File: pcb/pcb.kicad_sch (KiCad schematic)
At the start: 35 parts, among them J1 DIN-5_180degree, J5 Barrel_Jack, J6 Barrel_Jack, U1 MCP3008, U2 MCP3008

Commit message: completed circuit design
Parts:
- removed J5, J6, To_Main_Out: Barrel_Jack, symbol Connector:Barrel_Jack
- added C1, C2: C, symbol Device:C
- added J2: Conn_02x06_Odd_Even, Connector_PinHeader_2.54mm:PinHeader_2x06_P2.54mm_Horizontal, symbol Connector_Generic:Conn_02x06_Odd_Even
- added J3: Conn_02x02_Odd_Even, Connector_PinHeader_2.54mm:PinHeader_2x02_P2.54mm_Horizontal, symbol Connector_Generic:Conn_02x02_Odd_Even
- added R1: 220, symbol Device:R
- added R2: 270, symbol Device:R
- added U4: H11L1M, digikey-footprints:DIP-6_W7.62mm, symbol dk_Optoisolators-Logic-Output:H11L1M
- Bit_Crush_In1: renamed from Bit_Crush_In; symbol Connector:Barrel_Jack -> Connector_Audio:AudioJack2
- Bit_Crush_Out1: renamed from Bit_Crush_Out; symbol Connector:Barrel_Jack -> Connector_Audio:AudioJack2
- Delay_In1: renamed from Delay_In; symbol Connector:Barrel_Jack -> Connector_Audio:AudioJack2
- Delay_Out1: renamed from Delay_Out; symbol Connector:Barrel_Jack -> Connector_Audio:AudioJack2
- Distortion_In1: renamed from Distortion_In; symbol Connector:Barrel_Jack -> Connector_Audio:AudioJack2
- Distortion_Out1: renamed from Distortion_Out; symbol Connector:Barrel_Jack -> Connector_Audio:AudioJack2
- Filter_In1: renamed from Filter_In; symbol Connector:Barrel_Jack -> Connector_Audio:AudioJack2
- Filter_Out1: renamed from Filter_Out; symbol Connector:Barrel_Jack -> Connector_Audio:AudioJack2
- From_Sample1: renamed from From_Sample; symbol Connector:Barrel_Jack -> Connector_Audio:AudioJack2
- Reverb_In1: renamed from Reverb_In; symbol Connector:Barrel_Jack -> Connector_Audio:AudioJack2
- Reverb_Out1: renamed from Reverb_Out; symbol Connector:Barrel_Jack -> Connector_Audio:AudioJack2
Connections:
- net +3.3V: now also C1.1, C2.1, J2.1 (Pin_1), J2.2 (Pin_2), R2.1, U4.6 (VCC)
- net GND: now also C1.2, C2.2, J2.3 (Pin_3), J2.4 (Pin_4), U4.5 (GND)
- net at J1.4: now also R1.1
- net at J1.5: now also D3.2 (A), U4.2
- net at D3.1 (K): now also R1.2, U4.1
- net at U2.10 (~{CS}/SHDN): now also J2.6 (Pin_6)
- net at U1.11 (Din), U2.11 (Din): now also J3.4 (Pin_4)
- net at U1.12 (Dout), U2.12 (Dout): now also J3.3 (Pin_3)
- net at U1.13 (CLK), U2.13 (CLK): now also J3.1 (Pin_1)
- net at U1.10 (~{CS}/SHDN): now also J2.5 (Pin_5)
- new net: D2.1 (K), Reverb_In1.S, Reverb_In1.T
- new net: D6.1 (K), Distortion_In1.S, Distortion_In1.T
- new net: D6.2 (A), Distortion_Out1.S, Distortion_Out1.T, J2.10 (Pin_10)
- new net: J3.2 (Pin_2), R2.2, U4.4 (VO)
- new net: D5.1 (K), Filter_In1.S, Filter_In1.T
- new net: D5.2 (A), Filter_Out1.S, Filter_Out1.T, J2.8 (Pin_8)
- new net: D1.1 (K), Delay_In1.S, Delay_In1.T
- new net: D1.2 (A), Delay_Out1.S, Delay_Out1.T, J2.11 (Pin_11)
- new net: Bit_Crush_In1.S, Bit_Crush_In1.T, D4.1 (K)
- new net: Bit_Crush_Out1.S, Bit_Crush_Out1.T, D4.2 (A), J2.7 (Pin_7)
- new net: From_Sample1.S, From_Sample1.T, J2.12 (Pin_12)
- new net: D2.2 (A), J2.9 (Pin_9), Reverb_Out1.S, Reverb_Out1.T
- no-connect marks 6 -> 7
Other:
- moved on the sheet: D1, D2, J1

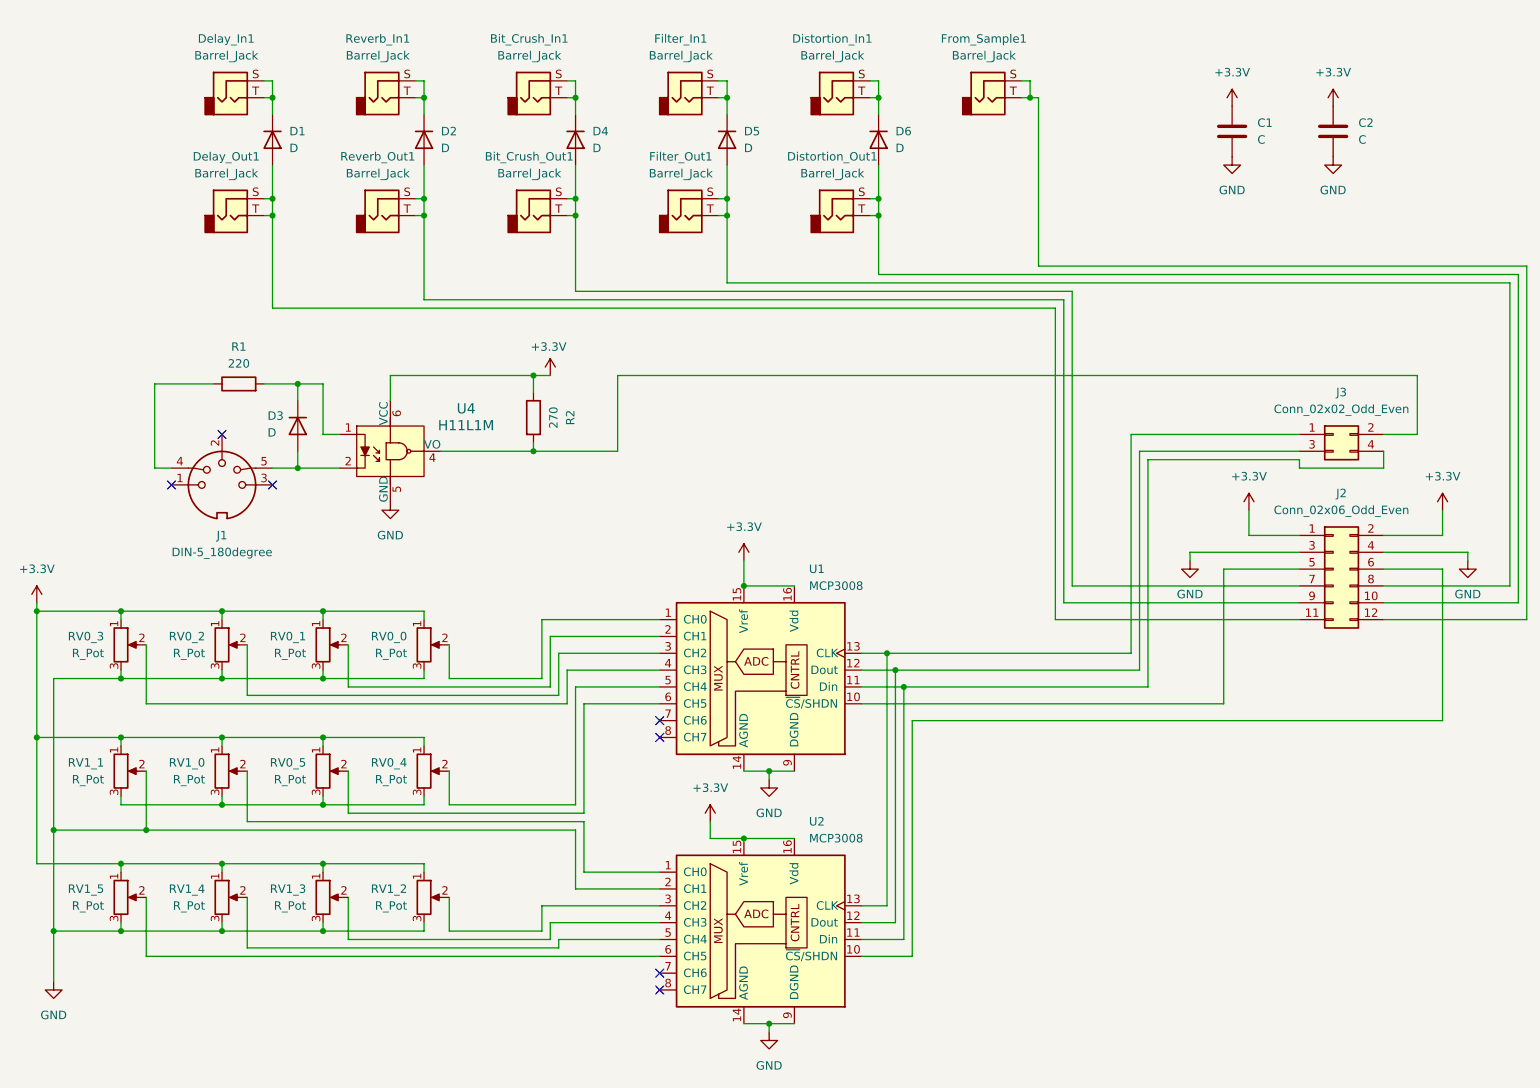
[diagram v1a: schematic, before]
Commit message: added footprints to pcb and updated gitignore to include kicad.gitignore
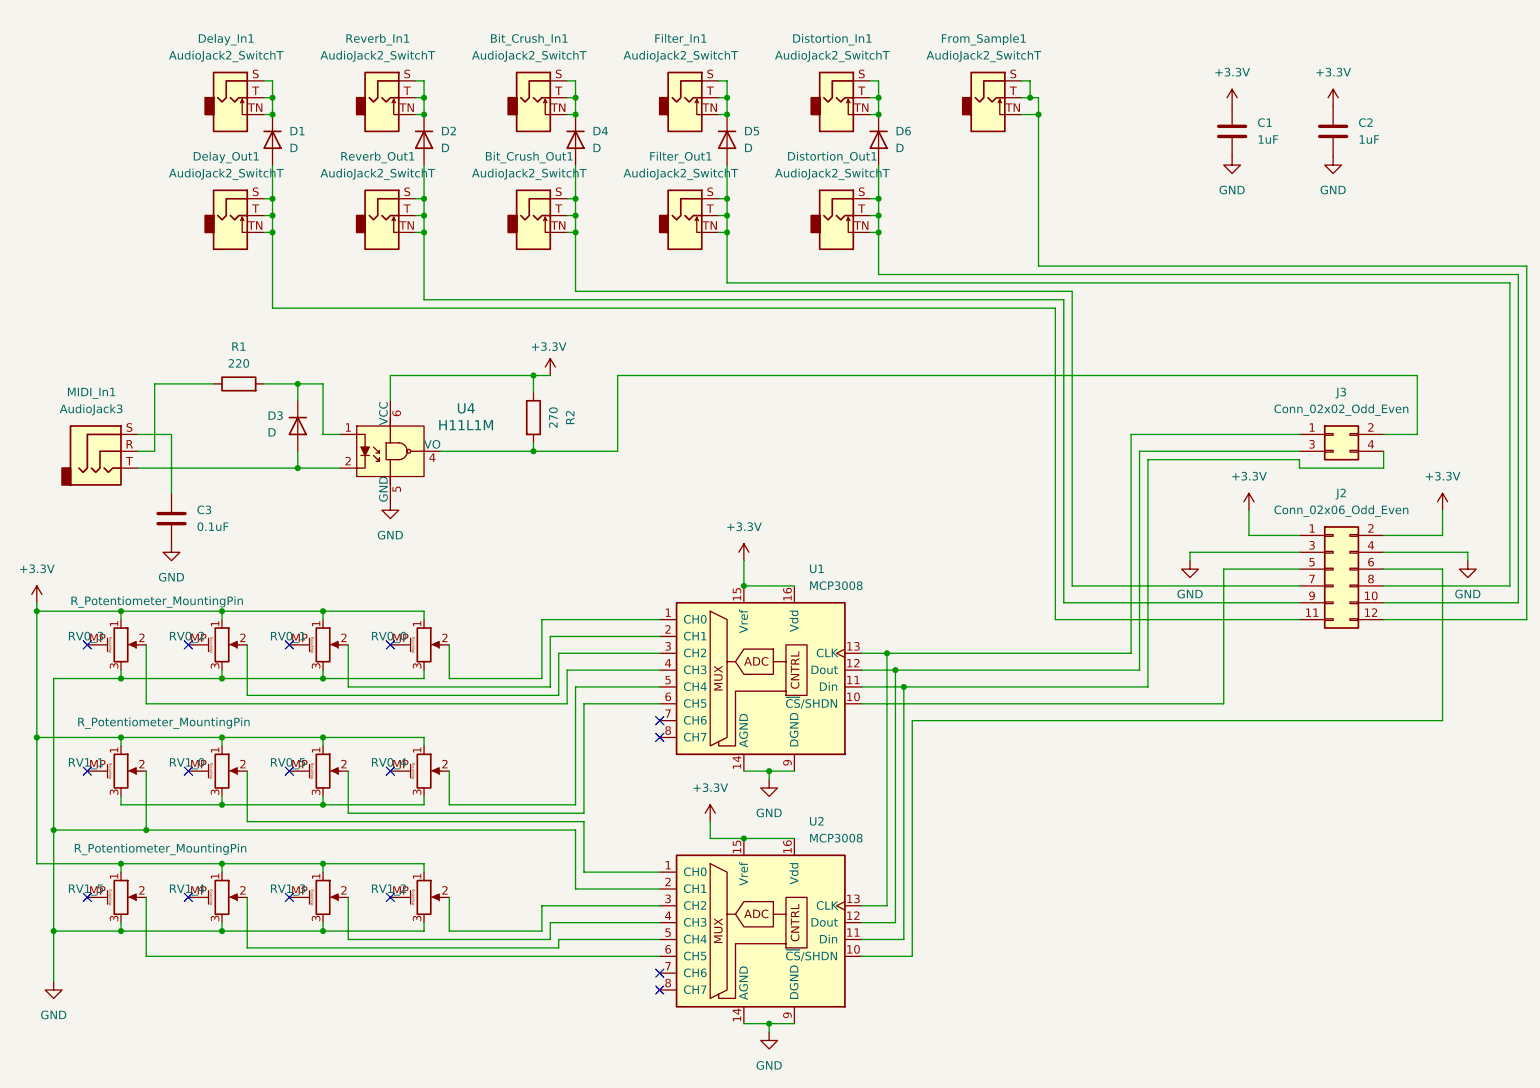
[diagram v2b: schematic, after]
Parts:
- removed J1: DIN-5_180degree, symbol Connector:DIN-5_180degree
- added C3: 0.1uF, digikey-footprints:0805, symbol Device:C
- added MIDI_In1: AudioJack3, My_Library:Jack_3.5mm_QingPu_WQP-PJ366ST_Vertical_CircularHoles, symbol Connector_Audio:AudioJack3
- Bit_Crush_In1, Bit_Crush_Out1, Delay_In1, Delay_Out1, Distortion_In1, Distortion_Out1, Filter_In1, Filter_Out1, From_Sample1, Reverb_In1, Reverb_Out1: value Barrel_Jack -> AudioJack2_SwitchT; footprint (none) -> Jack_3.5mm_QingPu_WQP-PJ398SM_Vertical_CircularHoles; symbol Connector_Audio:AudioJack2 -> Connector_Audio:AudioJack2_SwitchT
- C1, C2: value C -> 1uF; footprint (none) -> digikey-footprints:0805
- D1, D2, D3, D4, D5, D6, R1, R2: footprint (none) -> digikey-footprints:0805
- RV0_0, RV0_1, RV0_2, RV0_3, RV0_4, RV0_5, RV1_0, RV1_1, RV1_2, RV1_3, RV1_4, RV1_5: value R_Pot -> R_Potentiometer_MountingPin; footprint (none) -> My_Library:Potentiometer_Alpha_RD901F-40-00D_Single_Vertical_MP; symbol Device:R_Potentiometer -> Device:R_Potentiometer_MountingPin
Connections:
- net GND: now also C3.2
- net at D2.1 (K), Reverb_In1.S, Reverb_In1.T: now also Reverb_In1.TN
- net at R1.1: now also MIDI_In1.R
- net at D3.2 (A), U4.2: now also MIDI_In1.T
- net at D6.1 (K), Distortion_In1.S, Distortion_In1.T: now also Distortion_In1.TN
- net at D6.2 (A), Distortion_Out1.S, Distortion_Out1.T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: now also Distortion_Out1.TN
- net at D5.1 (K), Filter_In1.S, Filter_In1.T: now also Filter_In1.TN
- net at D5.2 (A), Filter_Out1.S, Filter_Out1.T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: now also Filter_Out1.TN
- net at D1.1 (K), Delay_In1.S, Delay_In1.T: now also Delay_In1.TN
- net at D1.2 (A), Delay_Out1.S, Delay_Out1.T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: now also Delay_Out1.TN
- net at Bit_Crush_In1.S, Bit_Crush_In1.T, D4.1 (K): now also Bit_Crush_In1.TN
- net at Bit_Crush_Out1.S, Bit_Crush_Out1.T, D4.2 (A)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: now also Bit_Crush_Out1.TN
- net at From_Sample1.S, From_Sample1.T, J2.12 (Pin_12): now also From_Sample1.TN
- net at D2.2 (A), J2.9 (Pin_9), Reverb_Out1.S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: now also Reverb_Out1.TN
- new net: C3.1, MIDI_In1.S
- no-connect marks 7 -> 16

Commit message: layed out pcb and adjusted design to meet Spartan 7 GPIO spec
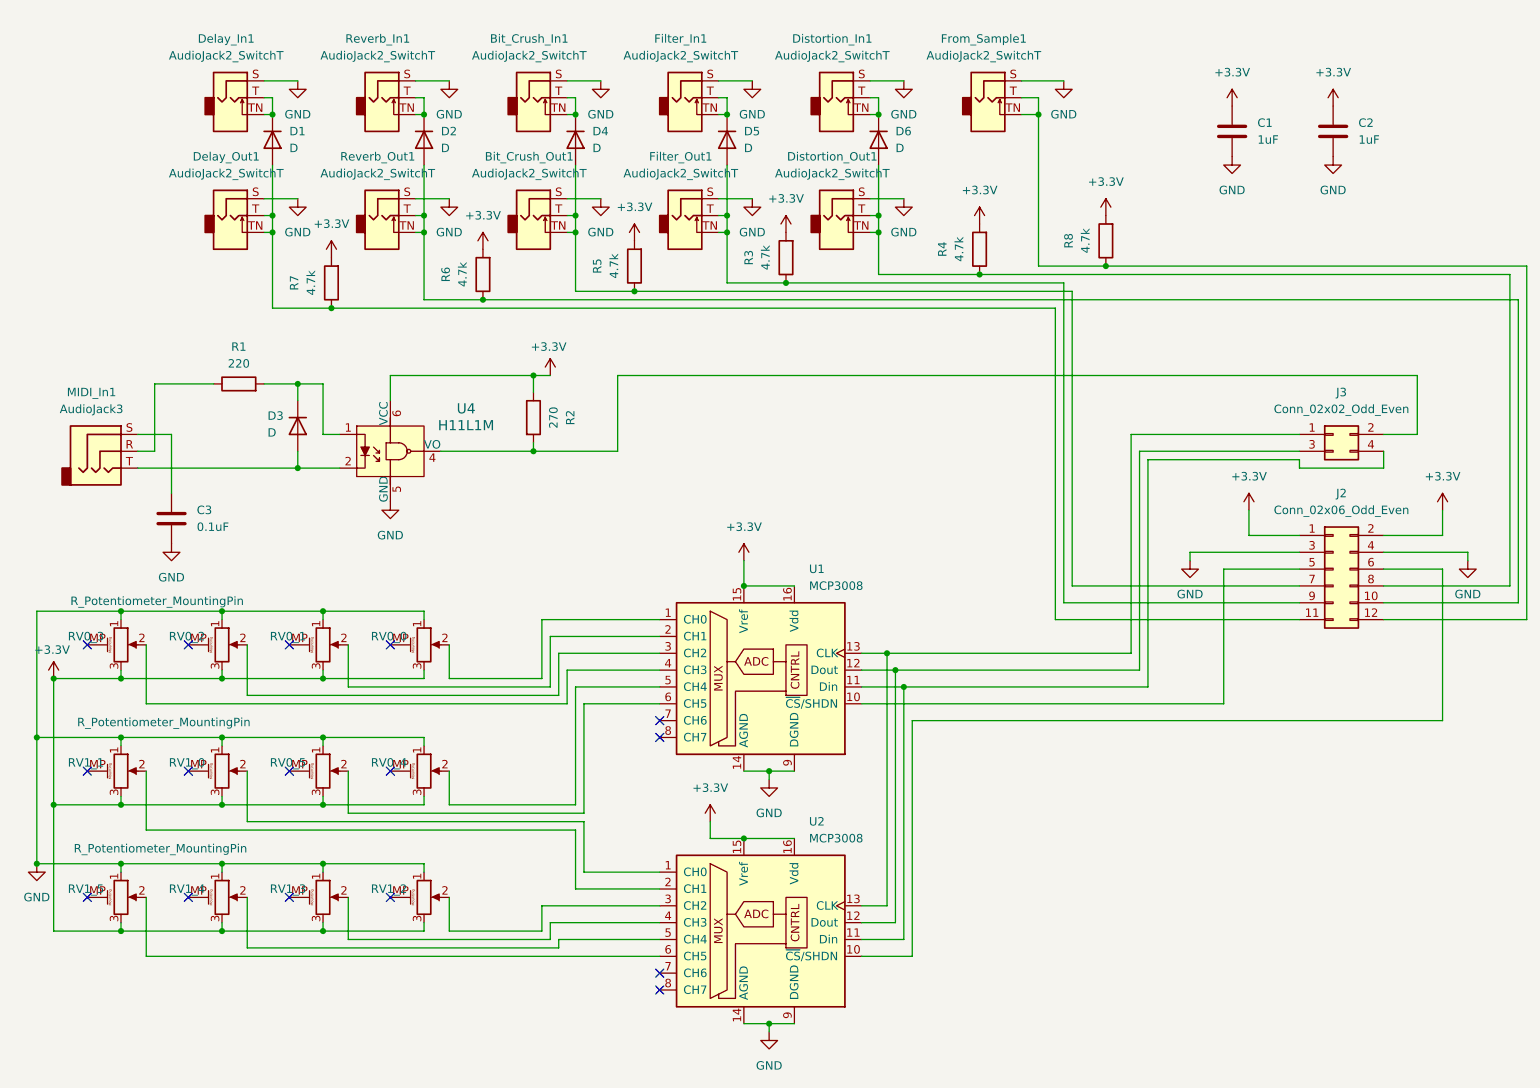
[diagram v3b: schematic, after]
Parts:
- added R3, R4, R5, R6, R7, R8: 4.7k, digikey-footprints:0805, symbol Device:R
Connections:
- net +3.3V: now also RV0_0.3, RV0_1.3, RV0_2.3, RV0_3.3, RV0_4.3, RV0_5.3, RV1_0.3, RV1_1.3, RV1_2.3, RV1_3.3, RV1_4.3, RV1_5.3, R3.2, R4.2, R5.2, R6.2, R7.2, R8.2; no longer RV0_0.1, RV0_1.1, RV0_2.1, RV0_3.1, RV0_4.1, RV0_5.1, RV1_0.1, RV1_1.1, RV1_2.1, RV1_3.1, RV1_4.1, RV1_5.1
- net GND: now also Bit_Crush_In1.S, Bit_Crush_Out1.S, Delay_In1.S, Delay_Out1.S, Distortion_In1.S, Distortion_Out1.S, Filter_In1.S, Filter_Out1.S, From_Sample1.S, RV0_0.1, RV0_1.1, RV0_2.1, RV0_3.1, RV0_4.1, RV0_5.1, RV1_0.1, RV1_1.1, RV1_2.1, RV1_3.1, RV1_4.1, RV1_5.1, Reverb_In1.S, Reverb_Out1.S; no longer RV0_0.3, RV0_1.3, RV0_2.3, RV0_3.3, RV1_1.2, RV1_2.3, RV1_3.3, RV1_4.3, RV1_5.3, U2.2 (CH1)
- net at D2.1 (K), Reverb_In1.T, Reverb_In1.TN: no longer Reverb_In1.S
- net at D6.1 (K), Distortion_In1.T, Distortion_In1.TN: no longer Distortion_In1.S
- net at D6.2 (A), Distortion_Out1.T, Distortion_Out1.TN: now also J2.8 (Pin_8), R4.1; no longer Distortion_Out1.S, J2.10 (Pin_10)
- net at D5.1 (K), Filter_In1.T, Filter_In1.TN: no longer Filter_In1.S
- net at D5.2 (A), Filter_Out1.T, Filter_Out1.TN: now also J2.9 (Pin_9), R3.1; no longer Filter_Out1.S, J2.8 (Pin_8)
- net at D1.1 (K), Delay_In1.T, Delay_In1.TN: no longer Delay_In1.S
- net at D1.2 (A), Delay_Out1.T, Delay_Out1.TN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: now also R7.1; no longer Delay_Out1.S
- net at Bit_Crush_In1.T, Bit_Crush_In1.TN, D4.1 (K): no longer Bit_Crush_In1.S
- net at Bit_Crush_Out1.T, Bit_Crush_Out1.TN, D4.2 (A)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: now also R5.1; no longer Bit_Crush_Out1.S
- net at From_Sample1.T, From_Sample1.TN, J2.12 (Pin_12): now also R8.1; no longer From_Sample1.S
- net at D2.2 (A), Reverb_Out1.T, Reverb_Out1.TN: now also J2.10 (Pin_10), R6.1; no longer J2.9 (Pin_9), Reverb_Out1.S
- new net: RV1_1.2, U2.2 (CH1)

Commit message: updated pcb based on schottky diodes availible from lab on floor 5
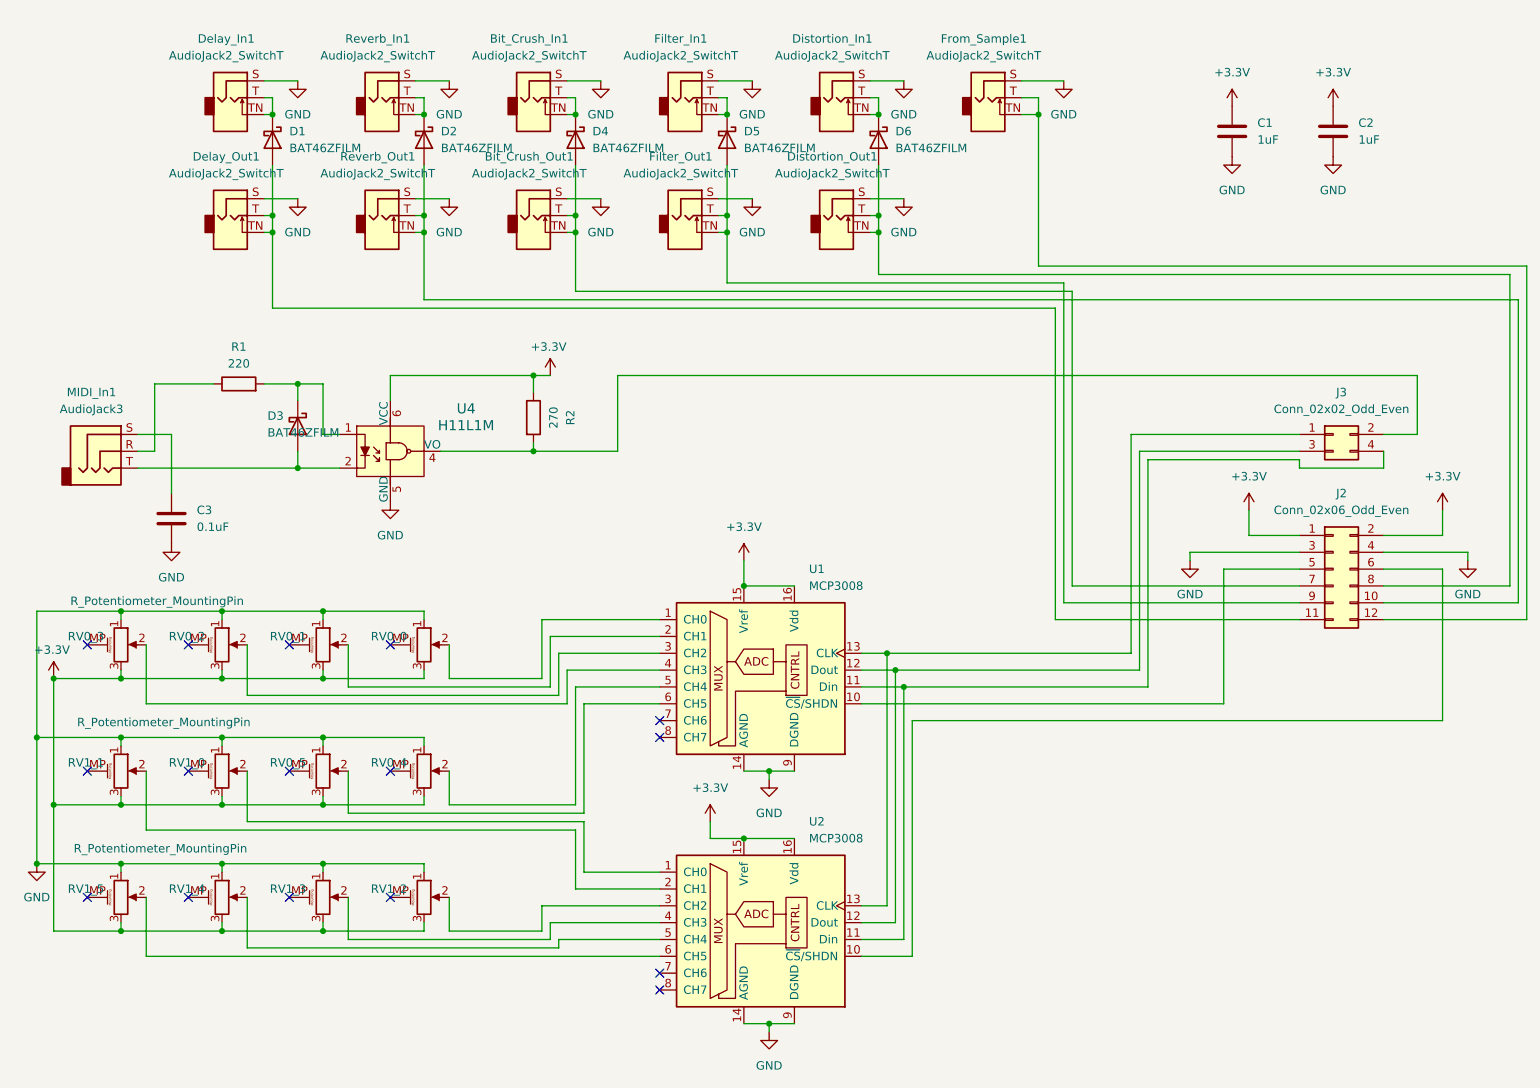
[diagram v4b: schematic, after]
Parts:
- removed R3, R4, R5, R6, R7, R8: 4.7k, digikey-footprints:0805, symbol Device:R
- D1, D2, D3, D4, D5, D6: value D -> BAT46ZFILM; footprint digikey-footprints:0805 -> Diode_SMD:D_SOD-123; symbol Device:D -> Diode:BAT46
